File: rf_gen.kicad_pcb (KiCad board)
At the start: 2 copper layers, 104.1 x 45.7 mm, 43 parts, among them J1 Conn_01x07_Male, J2 Conn_01x02_Female, J3 Conn_01x05_Male, J4 Jack-DC, Q1 GS61004B, Q2 G3R350MT12J, U1 NPC81074, U2 AP62150

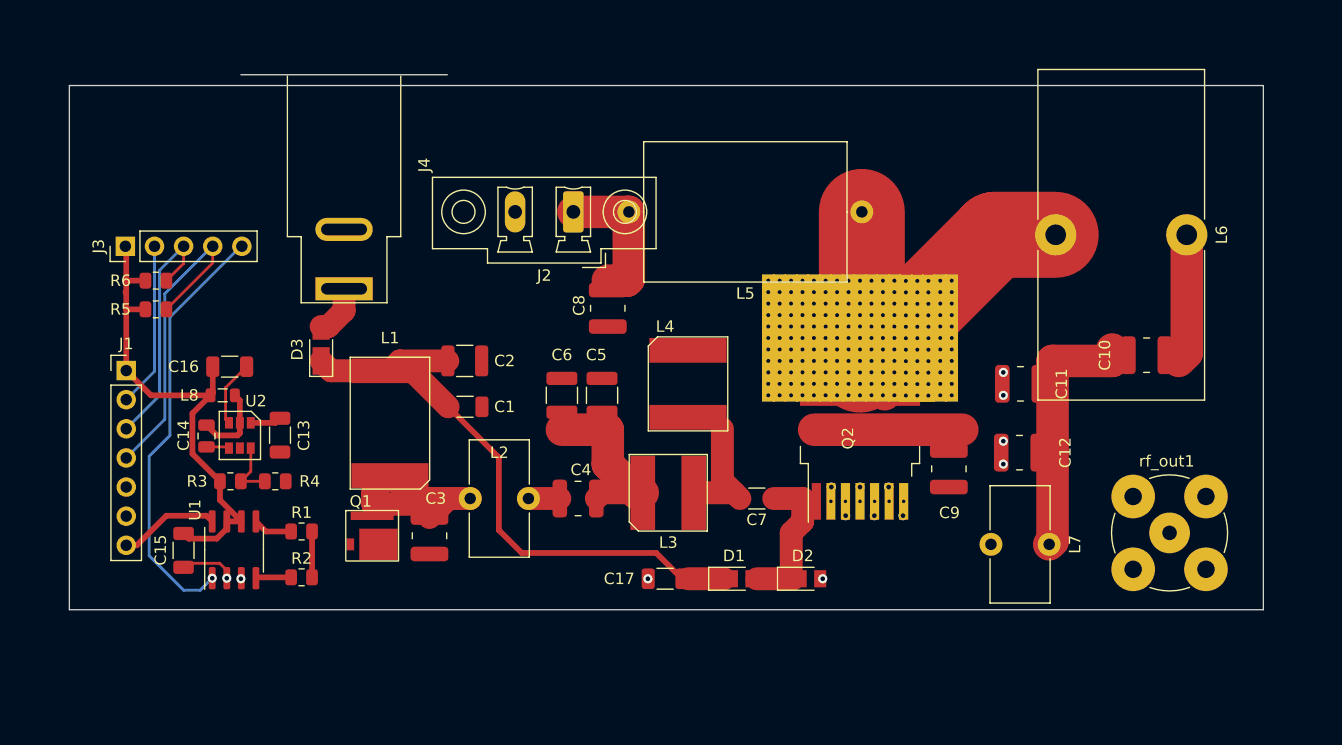
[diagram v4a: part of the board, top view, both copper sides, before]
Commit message: Finished routing
Replaced power inductor footprints with actual sizes
Placed test points that seemed useful, removed ones that didn't fit
Replaced RF connector and power input connectors
Added LED to indicate power
Added stitching vias
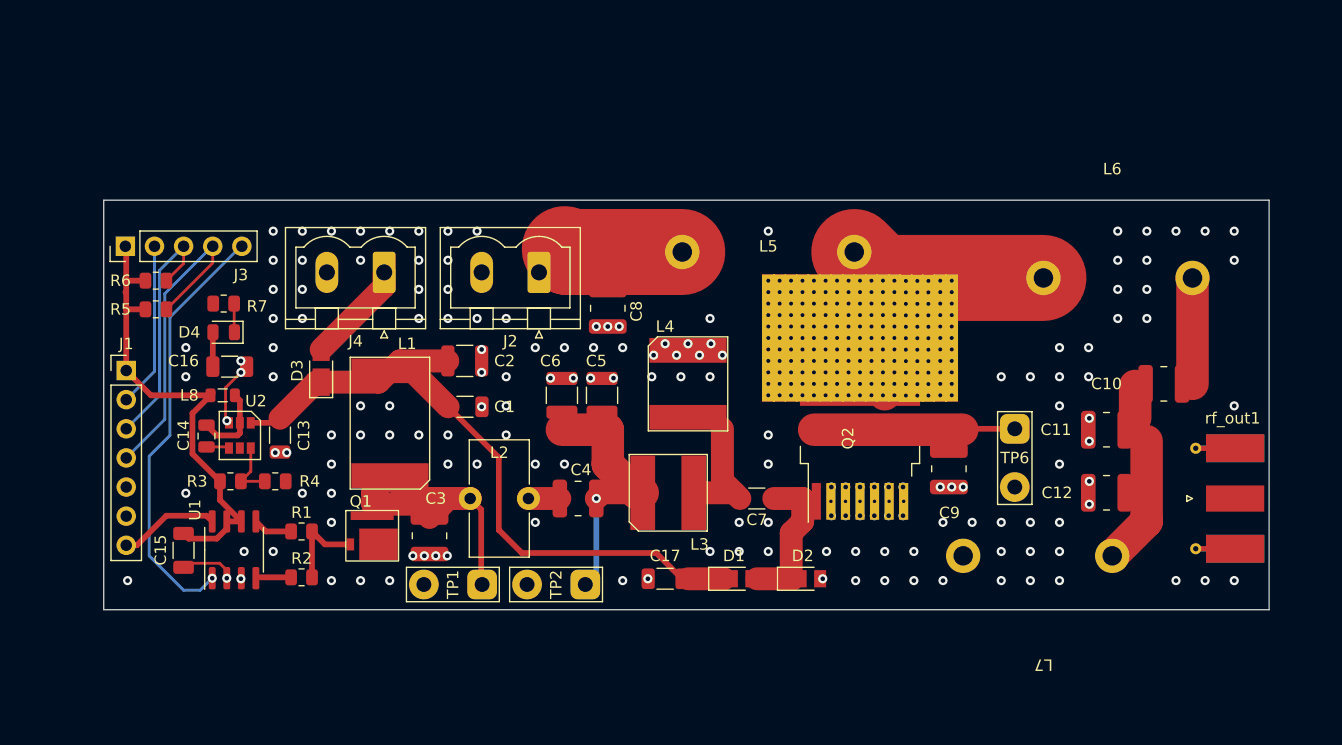
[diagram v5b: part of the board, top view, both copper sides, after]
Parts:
- added D4: LED, LED_SMD:LED_0805_2012Metric, F.Cu at (79.5, 115.5)
- added R7: 330, Resistor_SMD:R_0805_2012Metric, F.Cu at (79.5, 113.0)
- added TP1: test, TestPoint:TestPoint_2Pads_Pitch5.08mm_Drill1.3mm, F.Cu at (102.0, 137.5)
- added TP2: test, TestPoint:TestPoint_2Pads_Pitch5.08mm_Drill1.3mm, F.Cu at (111.0, 137.5)
- added TP6: test, TestPoint:TestPoint_2Pads_Pitch5.08mm_Drill1.3mm, F.Cu at (148.5, 123.9)
- J2: footprint Connector_Phoenix_MC_HighVoltage:PhoenixContact_MCV_1,5_2-GF-5.08_1x02_P5.08mm_Vertical_ThreadedFlange -> Connector_Phoenix_MSTB:PhoenixContact_MSTBVA_2,5_2-G_1x02_P5.00mm_Vertical
- J4: footprint Connector_BarrelJack:BarrelJack_SwitchcraftConxall_RAPC10U_Horizontal -> Connector_Phoenix_MSTB:PhoenixContact_MSTBVA_2,5_2-G_1x02_P5.00mm_Vertical
- L5: footprint Inductor_THT:L_Axial_L17.5mm_D12.0mm_P20.32mm_Horizontal_Vishay_IM-10-46 -> rf_gen:inductor_air_15x15
- L6: footprint Inductor_THT:L_Toroid_Vertical_L28.6mm_W14.3mm_P11.43mm_Bourns_5700 -> rf_gen:inductor_core_25x18
- L7: footprint Inductor_THT:L_Toroid_Vertical_L10.0mm_W5.0mm_P5.08mm -> rf_gen:inductor_core_25x18
- rf_out1: footprint Connector_Coaxial:BNC_TEConnectivity_1478204_Vertical -> Connector_Coaxial:SMA_Molex_73251-1153_EdgeMount_Horizontal
- moved L7 10.0 mm to (151.0, 144.0), turned to 180 degrees
- moved L5 8.88 mm to (127.0, 108.5), turned to 0 degrees
- moved C11 8.50 mm to (156.5, 124.0)
- moved C12 8.36 mm to (156.5, 129.5)
- moved L6 8.35 mm to (157.0, 101.8), turned to 0 degrees
- moved J2 6.07 mm to (107.0, 110.3)
- moved rf_out1 5.00 mm to (166.0, 130.0), turned to 180 degrees
- moved J4 3.78 mm to (93.5, 110.3), turned to 180 degrees
- moved C10 2.92 mm to (161.5, 120.0)
- moved D3 1.85 mm to (88.0, 119.0)
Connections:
- L5 pad 1: Net-(C9-Pad2) -> VDD
- L5 pad 2: VDD -> Net-(C9-Pad2)
- L6 pad 1: Net-(C10-Pad1) -> Net-(C9-Pad2)
- L6 pad 2: Net-(C9-Pad2) -> Net-(C10-Pad1)
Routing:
- net Net-(C9-Pad2): track 48.0 -> 38.2 mm
- net Net-(C10-Pad2): track 22.3 -> 14.1 mm
- net Net-(C3-Pad2): track 22.0 -> 29.9 mm
- net Net-(C4-Pad2): track 15.3 -> 23.2 mm, vias 0 -> 1
- net +12V: track 54.3 -> 59.3 mm
- net Net-(D3-Pad2): track 4.48 -> 9.00 mm
- net /GaN_gate: track 4.00 -> 7.81 mm
- net Net-(D4-Pad1): track 0.00 -> 2.51 mm
- net VDD: track 12.6 -> 10.4 mm
- net Net-(C10-Pad1): track 11.3 -> 9.24 mm
- net +5V: track 44.8 -> 45.5 mm
- net GND: vias 14 -> 162
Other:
- board size 104.1 x 45.7 mm -> 101.6 x 35.7 mm

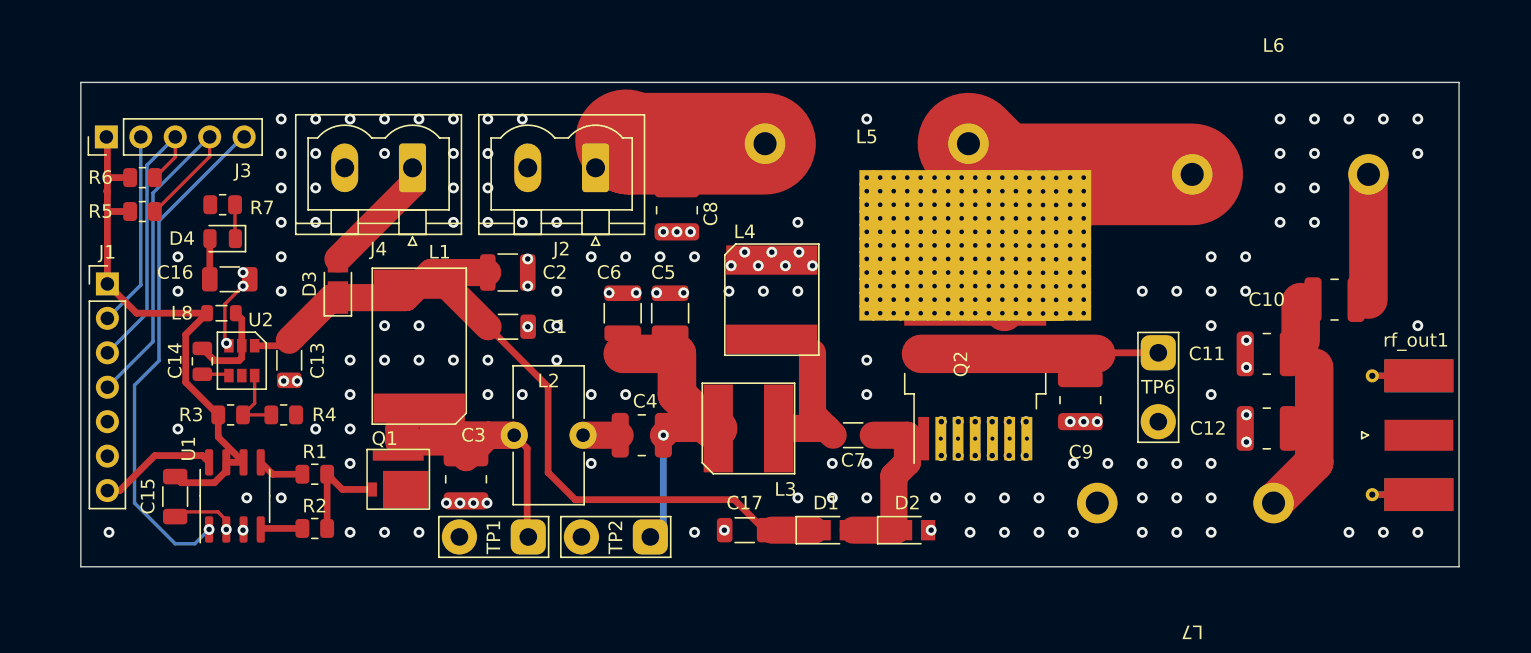
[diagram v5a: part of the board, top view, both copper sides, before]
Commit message: Added heatsink
Switched power inductors to surface-mount to avoid shorting
Added silkscreen text for connectors and LEDs
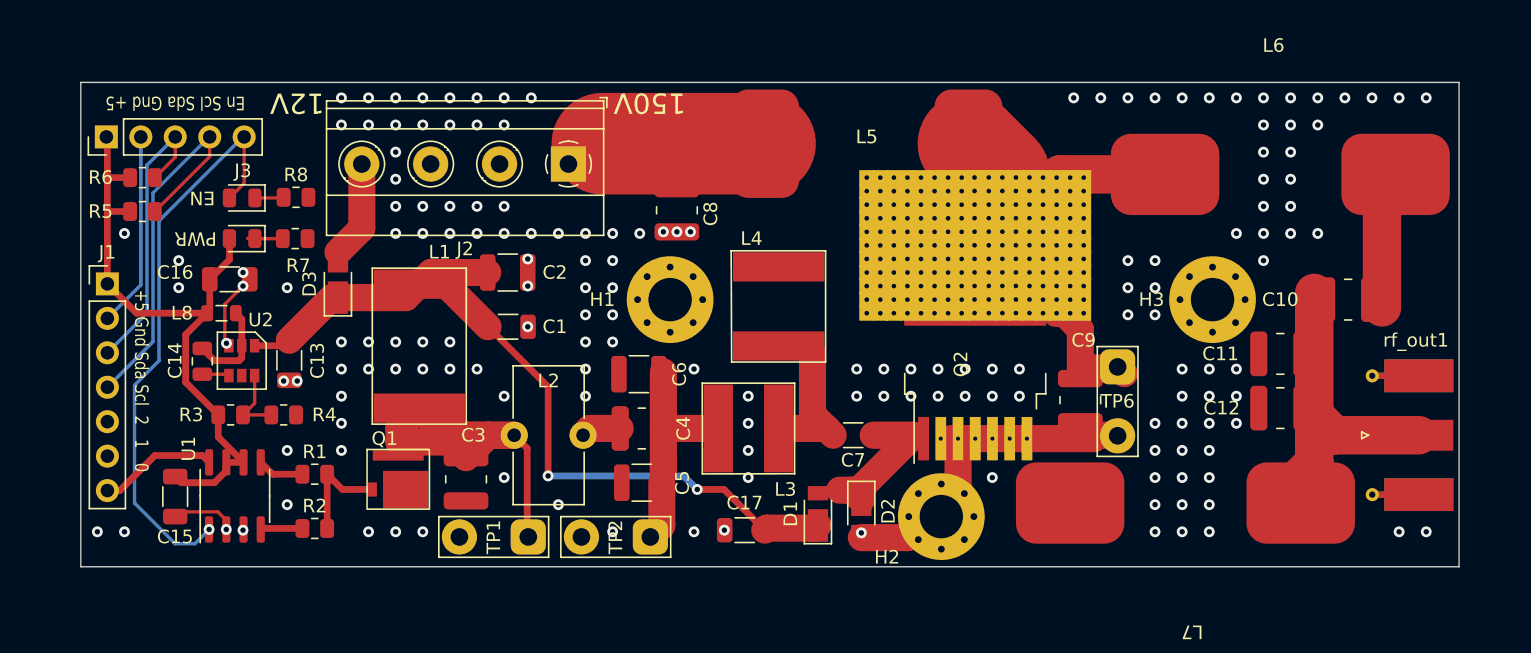
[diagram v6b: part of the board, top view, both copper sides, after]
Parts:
- removed J4: Jack-DC, Connector_Phoenix_MSTB:PhoenixContact_MSTBVA_2,5_2-G_1x02_P5.00mm_Vertical
- added EN: LED, LED_SMD:LED_0805_2012Metric, F.Cu at (80.9, 112.5)
- added H1: MountingHole_Pad, MountingHole:MountingHole_3.2mm_M3_Pad_Via, F.Cu at (112.5, 120.0)
- added H2: MountingHole_Pad, MountingHole:MountingHole_3.2mm_M3_Pad_Via, F.Cu at (132.5, 136.0)
- added H3: MountingHole_Pad, MountingHole:MountingHole_3.2mm_M3_Pad_Via, F.Cu at (152.5, 120.0)
- added R8: 330, Resistor_SMD:R_0805_2012Metric, F.Cu at (84.9, 112.5)
- J2: value Conn_01x02_Female -> Screw_Terminal_01x04; footprint Connector_Phoenix_MSTB:PhoenixContact_MSTBVA_2,5_2-G_1x02_P5.00mm_Vertical -> TerminalBlock_Phoenix:TerminalBlock_Phoenix_MKDS-1,5-4-5.08_1x04_P5.08mm_Horizontal
- moved C5 12.7 mm to (110.4, 133.5), turned to 180 degrees
- moved R7 5.91 mm to (84.8, 115.5), turned to 0 degrees
- moved C6 4.66 mm to (110.2, 125.5), turned to 180 degrees
- moved D2 3.68 mm to (126.6, 135.6), turned to -90 degrees
- moved TP6 3.18 mm to (145.5, 125.0)
- moved J2 2.02 mm to (105.0, 110.0)
- moved C12 1.80 mm to (157.5, 128.0)
- moved PWR 1.44 mm to (80.9, 115.5)
- moved D1 1.34 mm to (123.4, 135.8), turned to 90 degrees
- moved C10 1.00 mm to (162.5, 120.0)
- moved C11 1.00 mm to (157.5, 124.0)
- moved L4 0.71 mm to (120.5, 120.5)
- moved C4 0.50 mm to (110.4, 129.5)
- renumbered D4 to PWR
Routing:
- net GND: track 25.0 -> 49.7 mm, vias 162 -> 165
- net Net-(C9-Pad2): track 38.2 -> 24.9 mm
- net Net-(C10-Pad2): track 14.1 -> 25.1 mm
- net Net-(C4-Pad2): track 23.2 -> 17.6 mm, vias 1 -> 0
- net /EN: track 37.6 -> 42.5 mm
- net +5V: track 45.5 -> 48.3 mm
- net Net-(D5-Pad1): track 0.00 -> 2.14 mm
- net /SiC_gate: track 13.2 -> 11.2 mm
- net Net-(D3-Pad2): track 9.00 -> 7.23 mm
- net VDD: track 10.4 -> 12.0 mm
- net +12V: track 59.3 -> 60.3 mm, vias 0 -> 2
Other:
- board text added: "+5 Gnd Sda Scl 2 1 0"
- board text added: "12V"
- board text added: "150V"
- board text added: "En Scl Sda Gnd +5"

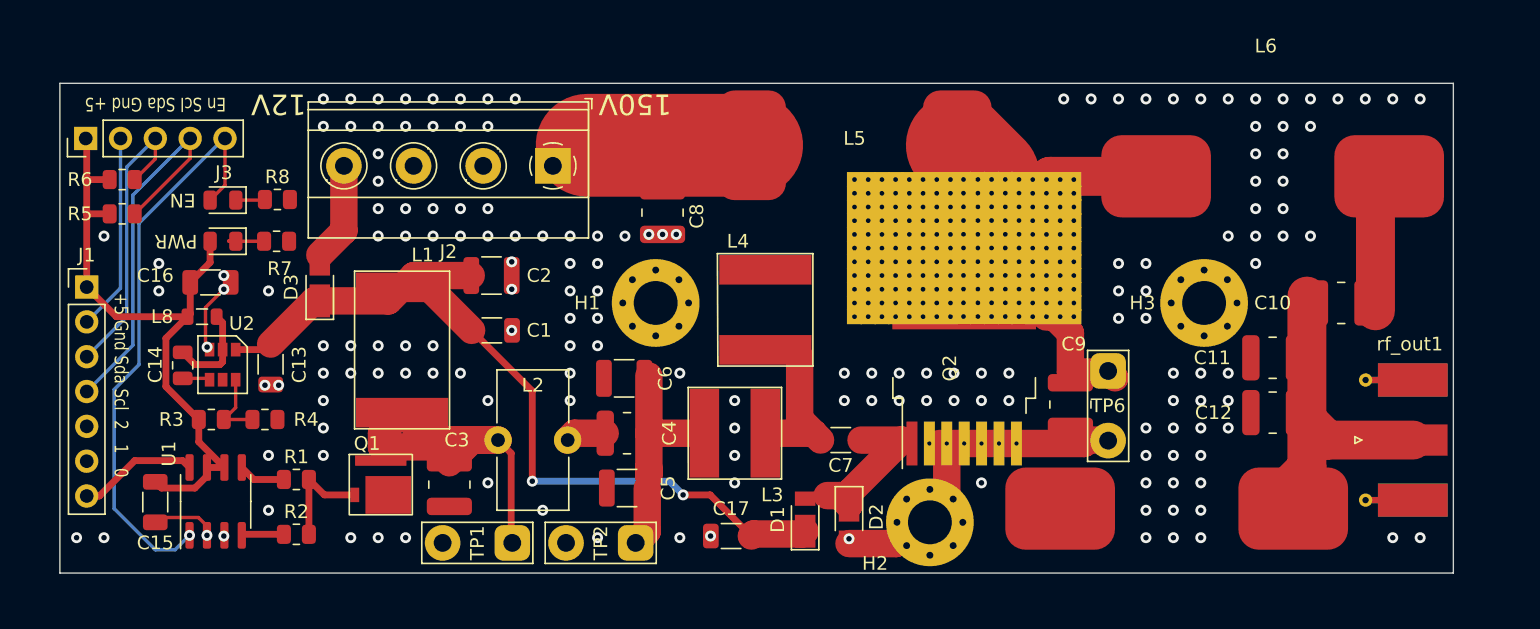
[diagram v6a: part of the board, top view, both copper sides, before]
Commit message: Finishing touches
Fixed design violations. Had to make exceptions for 1kV due to the dimensions of the parts
Added top and front views of PCB
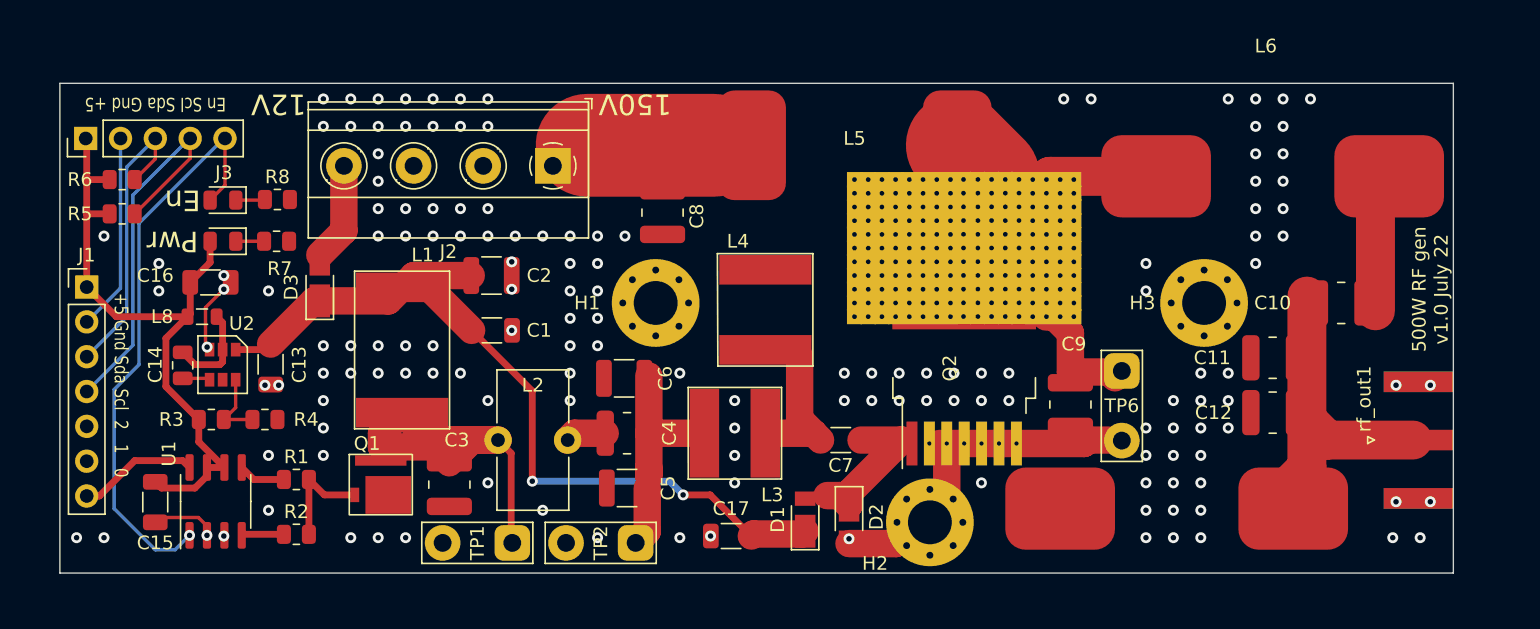
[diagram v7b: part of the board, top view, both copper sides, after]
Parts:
- rf_out1: footprint Connector_Coaxial:SMA_Molex_73251-1153_EdgeMount_Horizontal -> Connector_Coaxial:SMA_Amphenol_132289_EdgeMount
- moved rf_out1 2.14 mm to (168.1, 130.0), turned to 0 degrees
- moved TP6 1.00 mm to (146.5, 125.0)
- renumbered PWR to D4, EN to D5
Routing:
- net VDD: track 12.0 -> 9.25 mm
- net +12V: track 60.3 -> 58.4 mm
- net GND: track 49.7 -> 48.2 mm, vias 165 -> 149
- net Net-(C4-Pad2): track 17.6 -> 16.3 mm
- net +5V: track 48.3 -> 47.6 mm
- net Net-(D4-Pad1): track 2.60 -> 2.06 mm
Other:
- board text added: "500W RF gen v1.0 July 22"
- board text added: "En"
- board text added: "Pwr"

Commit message: Added 3D models for footprints
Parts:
- rf_out1: footprint Connector_Coaxial:SMA_Amphenol_132289_EdgeMount -> rf_gen:SMA_EdgeMount
- moved L7 5.22 mm to (149.5, 139.0)
- moved L6 4.27 mm to (157.5, 106.0)
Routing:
- net GND: vias 149 -> 145
